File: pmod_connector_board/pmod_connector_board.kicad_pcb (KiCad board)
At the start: 4 copper layers, 120 x 15 mm, 4 parts, among them J1 Conn_02x06_Top_Bottom, J2 Conn_02x06_Top_Bottom, J3 Conn_02x06_Top_Bottom, J4 Conn_02x06_Top_Bottom

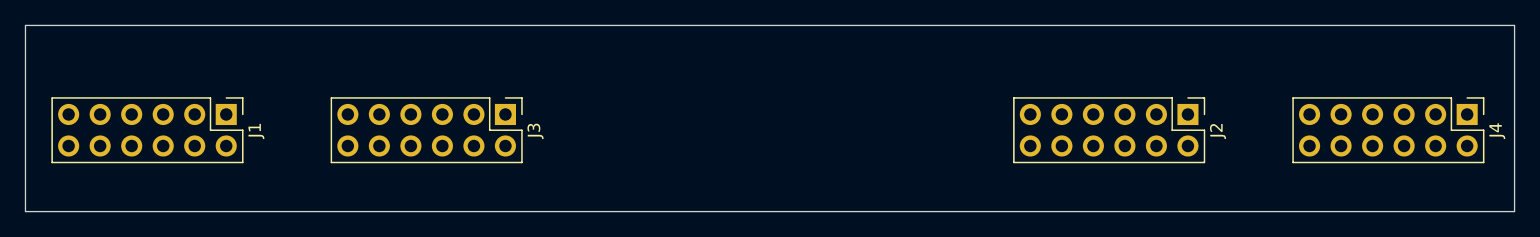
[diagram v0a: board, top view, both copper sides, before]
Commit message: finish place and route. Reduce board size
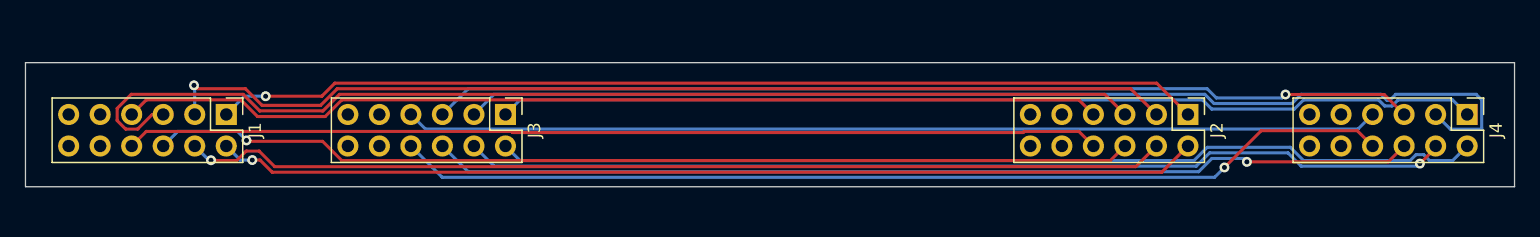
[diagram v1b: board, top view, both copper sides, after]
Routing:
- net Net-(J3-Pad2): track 0.00 -> 89.6 mm
- net Net-(J1-Pad3): track 0.00 -> 88.9 mm
- net Net-(J1-Pad2): track 0.00 -> 82.0 mm, vias 0 -> 1
- net Net-(J3-Pad10): track 0.00 -> 80.6 mm, vias 0 -> 1
- net Net-(J3-Pad8): track 0.00 -> 79.8 mm, vias 0 -> 1
- net Net-(J3-Pad7): track 0.00 -> 79.8 mm
- net Net-(J1-Pad1): track 0.00 -> 79.6 mm, vias 0 -> 1
- net Net-(J1-Pad4): track 0.00 -> 79.6 mm
- net Net-(J1-Pad8): track 0.00 -> 79.5 mm, vias 0 -> 1
- net Net-(J3-Pad1): track 0.00 -> 79.5 mm
- net Net-(J1-Pad9): track 0.00 -> 79.4 mm, vias 0 -> 1
- net Net-(J3-Pad3): track 0.00 -> 79.4 mm, vias 0 -> 1
- net Net-(J3-Pad9): track 0.00 -> 79.4 mm, vias 0 -> 1
- net Net-(J1-Pad7): track 0.00 -> 79.3 mm, vias 0 -> 1
- net Net-(J1-Pad10): track 0.00 -> 78.5 mm
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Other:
- board size 120 x 15 mm -> 120 x 10 mm

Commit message: finish PMOD connector PCB
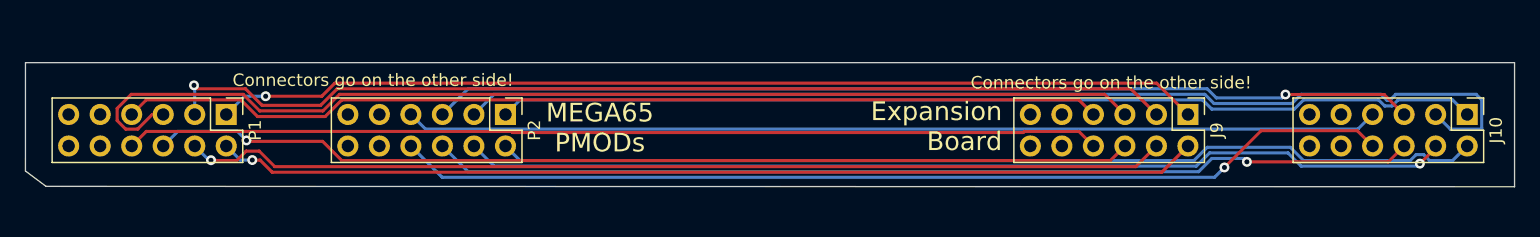
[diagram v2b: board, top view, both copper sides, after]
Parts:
- renumbered J4 to J10, J2 to J9, J1 to P1, J3 to P2
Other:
- outline, holes or cut-outs redrawn
- board text added: "Connectors go on the other side!"
- board text added: "Connectors go on this side"
- board text added: "Expansion Board"
- board text added: "MEGA65 Expansion Board PMOD Bridge, revA (C) Paul Gardner-Stephen 2024, CC-BY 4.0"
- board text added: "MEGA65 PMODs"
